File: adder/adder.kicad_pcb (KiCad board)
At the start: 2 copper layers, 52.9 x 21.5 mm, 29 parts

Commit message: Started on adder v3
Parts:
- removed A1: LA1, LEDs:LED_0805_HandSoldering
- removed A1: A1, library:mini-vertical-slide-switch
- removed A2: LA2, LEDs:LED_0805_HandSoldering
- removed A2: A2, library:mini-vertical-slide-switch
- removed A3: LA3, LEDs:LED_0805_HandSoldering
- removed A3: A3, library:mini-vertical-slide-switch
- removed A4: A4, LEDs:LED_0805_HandSoldering
- removed A4: A4, library:mini-vertical-slide-switch
- removed AND (x2): AND, library:ssop14
- removed B1: LB1, LEDs:LED_0805_HandSoldering
- removed B1: B1, library:mini-vertical-slide-switch
- removed B2: LB2, LEDs:LED_0805_HandSoldering
- removed B2: B2, library:mini-vertical-slide-switch
- removed B3: LB3, LEDs:LED_0805_HandSoldering
- removed B3: B3, library:mini-vertical-slide-switch
- removed B4: LB4, LEDs:LED_0805_HandSoldering
- removed B4: B4, library:mini-vertical-slide-switch
- removed CIN: VIN, Pin_Headers:Pin_Header_Straight_1x03_Pitch2.54mm
- removed COUT: VOUT, Pin_Headers:Pin_Header_Straight_1x03_Pitch2.54mm
- removed OR: OR, library:ssop14
- removed S1: S1, LEDs:LED_0805_HandSoldering
- removed S2: S2, LEDs:LED_0805_HandSoldering
- removed S3: S3, LEDs:LED_0805_HandSoldering
- removed S4: S4, LEDs:LED_0805_HandSoldering
- removed VIN: A, Pin_Headers:Pin_Header_Straight_1x04_Pitch2.54mm
- removed VOUT: B, Pin_Headers:Pin_Header_Straight_1x04_Pitch2.54mm
- removed XOR (x2): XOR, library:ssop14
- added D1: A1, LEDs:LED_0805_HandSoldering, F.Cu at (134.4, 94.1)
- added D10: S2, LEDs:LED_0805_HandSoldering, F.Cu at (123.0, 101.0)
- added D11: S3, LEDs:LED_0805_HandSoldering, F.Cu at (115.4, 101.0)
- added D12: S4, LEDs:LED_0805_HandSoldering, F.Cu at (107.8, 101.0)
- added D2: B1, LEDs:LED_0805_HandSoldering, F.Cu at (115.4, 94.1)
- added D3: A2, LEDs:LED_0805_HandSoldering, F.Cu at (130.6, 94.1)
- added D4: B2, LEDs:LED_0805_HandSoldering, F.Cu at (111.6, 94.1)
- added D5: A3, LEDs:LED_0805_HandSoldering, F.Cu at (126.8, 94.1)
- added D6: B3, LEDs:LED_0805_HandSoldering, F.Cu at (107.8, 94.1)
- added D7: A4, LEDs:LED_0805_HandSoldering, F.Cu at (123.0, 94.1)
- added D8: B4, LEDs:LED_0805_HandSoldering, F.Cu at (104.0, 94.1)
- added D9: S1, LEDs:LED_0805_HandSoldering, F.Cu at (130.6, 101.0)
- added J1: AIN, Socket_Strips:Socket_Strip_Straight_1x04_Pitch2.54mm, F.Cu at (138.2, 80.0)
- added J2: BIN, Socket_Strips:Socket_Strip_Straight_1x04_Pitch2.54mm, F.Cu at (100.0, 80.0)
- added J3: VIN, Socket_Strips:Socket_Strip_Straight_1x03_Pitch2.54mm, F.Cu at (138.2, 94.5)
- added J4: VOUT, Socket_Strips:Socket_Strip_Straight_1x03_Pitch2.54mm, F.Cu at (100.0, 94.5)
- added J5: SOUT, Socket_Strips:Socket_Strip_Straight_1x04_Pitch2.54mm, F.Cu at (123.0, 105.3)
- added R1: R, Resistors_SMD:R_0805_HandSoldering, F.Cu at (134.4, 89.3)
- added R10: S2, Resistors_SMD:R_0805_HandSoldering, F.Cu at (123.0, 98.5)
- added R11: S3, Resistors_SMD:R_0805_HandSoldering, F.Cu at (115.4, 98.5)
- added R12: S4, Resistors_SMD:R_0805_HandSoldering, F.Cu at (107.8, 98.5)
- added R2: R, Resistors_SMD:R_0805_HandSoldering, F.Cu at (115.4, 89.3)
- added R3: R, Resistors_SMD:R_0805_HandSoldering, F.Cu at (130.6, 89.3)
- added R4: R, Resistors_SMD:R_0805_HandSoldering, F.Cu at (111.6, 89.3)
- added R5: R, Resistors_SMD:R_0805_HandSoldering, F.Cu at (126.8, 89.3)
- added R6: R, Resistors_SMD:R_0805_HandSoldering, F.Cu at (107.8, 89.3)
- added R7: R, Resistors_SMD:R_0805_HandSoldering, F.Cu at (123.0, 89.3)
- added R8: R, Resistors_SMD:R_0805_HandSoldering, F.Cu at (104.0, 89.3)
- added R9: S1, Resistors_SMD:R_0805_HandSoldering, F.Cu at (130.6, 98.5)
- added U1: A1, library:mini-vertical-slide-switch, F.Cu at (134.4, 82.5)
- added U10: A4, library:mini-vertical-slide-switch, F.Cu at (123.0, 82.5)
- added U11: B4, library:mini-vertical-slide-switch, F.Cu at (104.0, 82.5)
- added U12: AND, library:ssop14, B.Cu at (106.5, 91.8)
- added U13: OR, library:ssop14, B.Cu at (119.2, 96.0)
- added U2: B1, library:mini-vertical-slide-switch, F.Cu at (115.4, 82.5)
- added U3: XOR, library:ssop14, B.Cu at (106.5, 102.5)
- added U4: A2, library:mini-vertical-slide-switch, F.Cu at (130.6, 82.5)
- added U5: B2, library:mini-vertical-slide-switch, F.Cu at (111.6, 82.5)
- added U6: XOR, library:ssop14, B.Cu at (131.7, 91.8)
- added U7: A3, library:mini-vertical-slide-switch, F.Cu at (126.8, 82.5)
- added U8: B3, library:mini-vertical-slide-switch, F.Cu at (107.8, 82.5)
- added U9: AND, library:ssop14, B.Cu at (131.7, 102.5)
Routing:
- net VCC: track 132.8 -> 0.00 mm, vias 1 -> 0
- net +5V: track 0.00 -> 81.6 mm
- net /A1: track 26.5 -> 84.8 mm, vias 0 -> 1
- net /S4: track 12.0 -> 62.0 mm, vias 1 -> 0
- net GND: track 115.3 -> 164.9 mm, vias 2 -> 3
- net /A4: track 95.4 -> 51.0 mm, vias 0 -> 1
- net /XAB4: track 0.00 -> 41.8 mm
- net /COUT: track 31.2 -> 72.7 mm, vias 0 -> 1
- net /A2: track 49.7 -> 88.4 mm, vias 0 -> 1
- net /XAB2: track 0.00 -> 38.2 mm
- net /B3: track 29.7 -> 66.7 mm
- net /XAB1: track 0.00 -> 33.9 mm
- net /XAB3: track 0.00 -> 32.7 mm
- net /S1: track 3.72 -> 35.6 mm, vias 1 -> 0
- net /B1: track 59.9 -> 89.9 mm, vias 0 -> 2
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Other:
- board size 52.9 x 21.5 mm -> 42 x 29.3 mm
- board text removed: "CIN"
- board text removed: "COUT"
- board text removed: "GND"
- board text removed: "VCC"

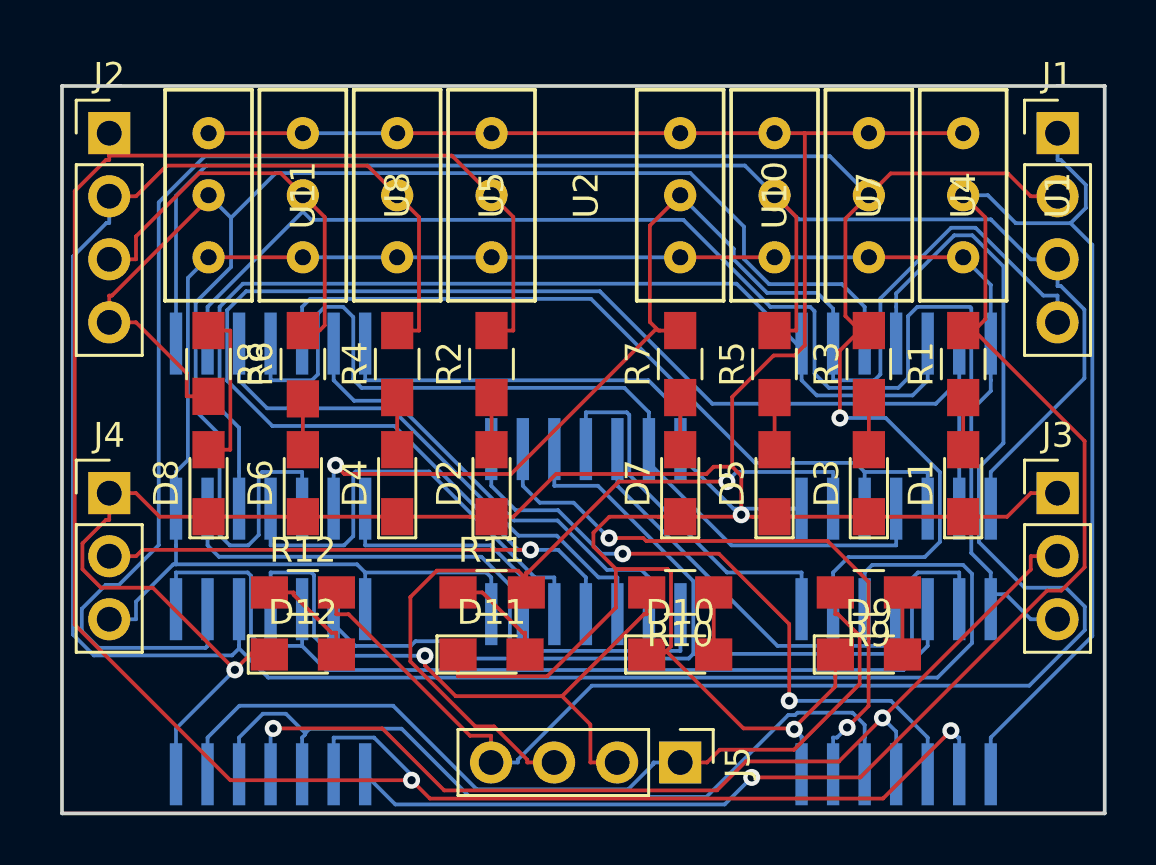
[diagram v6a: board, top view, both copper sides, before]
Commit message: Updated adder
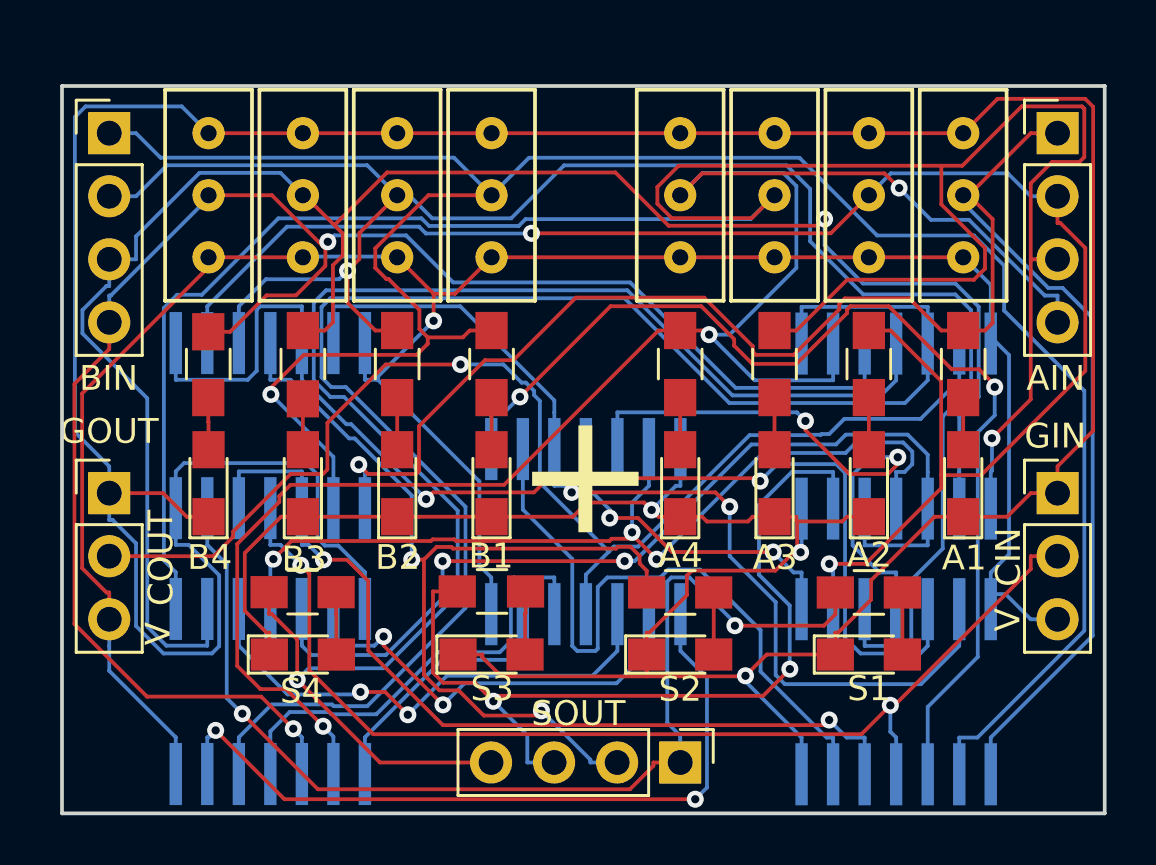
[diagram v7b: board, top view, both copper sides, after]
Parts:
- AND: renamed from U12; value AND -> ANDB
- moved XORB 10.7 mm to (106.5, 91.8)
- moved AND 10.7 mm to (106.5, 102.5)
- turned R11 to 180 degrees
- turned R12 to 180 degrees
- turned R8 to 90 degrees
- renumbered D1 to A1, D3 to A2, D5 to A3, D7 to A4, J1 to AIN, U9 to ANDA, D2 to B1, D4 to B2, D6 to B3, D8 to B4, J2 to BIN, J3 to GIN, J4 to GOUT, U1 to IA1, U4 to IA2, U7 to IA3, U10 to IA4, U2 to IB1, U5 to IB2, U8 to IB3, U11 to IB4, U13 to OR, D9 to S1, D10 to S2, D11 to S3, D12 to S4, J5 to SOUT, U6 to XORA, U3 to XORB
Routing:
- net /A3: track 62.4 -> 97.4 mm, vias 0 -> 1
- net GND: track 164.9 -> 189.6 mm
- net /A4: track 51.0 -> 73.4 mm, vias 1 -> 3
- net /XAB4: track 41.8 -> 63.9 mm
- net /COUT: track 72.7 -> 51.1 mm
- net /A2: track 88.4 -> 69.4 mm, vias 1 -> 2
- net /AAB1: track 26.6 -> 43.8 mm
- net /B2: track 85.8 -> 72.5 mm, vias 0 -> 1
- net /A1: track 84.8 -> 72.3 mm
- net +5V: track 81.6 -> 92.5 mm, vias 0 -> 1
- net /XAB2: track 38.2 -> 48.7 mm, vias 0 -> 2
- net /S2: track 26.8 -> 37.0 mm, vias 1 -> 2
- net /B3: track 66.7 -> 76.5 mm, vias 0 -> 1
- net /S1: track 35.6 -> 44.6 mm, vias 0 -> 2
- net /XAB3: track 32.7 -> 39.4 mm, vias 0 -> 2
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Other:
- board text added: "+"
- board text added: "CIN"
- board text added: "COUT"
- board text added: "V"
